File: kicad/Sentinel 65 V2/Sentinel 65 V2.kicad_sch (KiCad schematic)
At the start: 159 parts, among them J1 SNES Controller, J10 SVGA Connector, J11 USB_C_Receptacle_PowerOnly_6P, J12 Conn_01x02, J13 Conn_01x02, J14 Internal Control Header (Opti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, J15 Conn_02x11_Odd_Even, J2 2x32 2.54mm Card Edge Connect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, J3 Conn_02x12_Odd_Even, J4 SNES Controller, J5 SD_Card, J6 LEFT, J7 FPGA_PROG, J8 RIGHT, J9 Flash Enable, SW1 SW_Push, SW2 SW_Push, SW3 SW_Push, U1 ATF22LV10C, U10 LM1086IT-3.3, U11 MCP1316MT-33LE/OT, U2 W65C265S8PLG-8, U3 IS61WV5128EDBLL-10TLI, U4 SST39LF040-55-4C-NHE-T, U5 W25Q16JVSNIQ, U6 AP7361C-12E, U7 74CBTLV3126PW,118, U8 ICE40UP5K-SG48ITR, U9 WM8524CGEDT, X1 32.768KHz, X2 8Mhz, X3 25MHz

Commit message: Added audio mixing of cartridge audio
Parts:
- removed C26: 1µF, Capacitor_SMD:C_0402_1005Metric, symbol Device:C
- removed C27: 2.7nf, Capacitor_SMD:C_0402_1005Metric, symbol Device:C
- removed C29: 2.2µF, Capacitor_SMD:C_0402_1005Metric, symbol Device:C
- removed C31, C32: 4.7µF, Capacitor_SMD:C_0402_1005Metric, symbol Device:C
- removed D1, D2: PESD3V3L1BA-N, Diode_SMD:D_SOD-323, symbol Diode:PESD3V3L1BA-N
- removed J6: LEFT, symbol Connector:Conn_Coaxial
- removed J8: RIGHT, symbol Connector:Conn_Coaxial
- removed J9: Flash Enable, Connector_PinHeader_2.54mm:PinHeader_1x02_P2.54mm_Vertical, symbol Connector_Generic:Conn_01x02
- removed JP1: Jumper_3_Open, Jumper:SolderJumper-3_P2.0mm_Open_TrianglePad1.0x1.5mm_NumberLabels, symbol Jumper:Jumper_3_Open
- removed R12, R19: 560Ω, Resistor_SMD:R_0402_1005Metric, symbol Device:R
- removed R24, R48: 3.3kΩ, Resistor_SMD:R_0402_1005Metric, symbol Device:R
- added C26, C27, C29, C31, C32, C33: 2.2µF, symbol Device:C_Polarized
- added C34: 2.2µF, Capacitor_SMD:C_0402_1005Metric, symbol Device:C
- added C35: 1µF, Capacitor_SMD:C_0402_1005Metric, symbol Device:C
- added C36, C37: 4.7µF, Capacitor_SMD:C_0402_1005Metric, symbol Device:C
- added D10, D11: PESD3V3L1BA-N, Diode_SMD:D_SOD-323, symbol Diode:PESD3V3L1BA-N
- added J12: LEFT, symbol Connector:Conn_Coaxial
- added J13: RIGHT, symbol Connector:Conn_Coaxial
- added JP1: SolderJumper_3_Bridged12, Jumper:SolderJumper-3_P1.3mm_Bridged12_RoundedPad1.0x1.5mm, symbol Jumper:SolderJumper_3_Bridged12
- added R57, R58, R60, R61: 3.3kΩ, Resistor_SMD:R_0402_1005Metric, symbol Device:R
- added R71, R72, R73, R74, R75, R76: 1kΩ, Resistor_SMD:R_0402_1005Metric, symbol Device:R
- added U10: TLV9062xD, Package_SO:SOIC-8_3.9x4.9mm_P1.27mm, symbol Amplifier_Operational:TLV9062xD
- C28: value 2.7nF -> 1µF
- C30: value 1µF -> 100nF
- J10: renamed from J13; now fitted; now in the parts list
- J11: renamed from J12; now fitted; now in the parts list
- renumbered C37 to C38, C33 to C39, C34 to C40, C35 to C41, C36 to C42, C8 to C5, C5 to C8, D6 to D1, D8 to D2, D7 to D3, D9 to D4, D13 to D5, D12 to D6, D3 to D7, D4 to D8, D5 to D9, H6 to H1, H5 to H2, H4 to H3, H3 to H4, H2 to H5, H1 to H6, J11 to J14, J4 to J2, J2 to J3, J3 to J4, J14 to J5, J15 to J6, J5 to J7, J7 to J8, J10 to J9, R13 to R12, R14 to R13, R15 to R14, R16 to R15, R17 to R16, R18 to R17, R26 to R18, R25 to R19, R28 to R24, R27 to R25, R31 to R26, R29 to R27, R30 to R28, R37 to R29, R32 to R30, R64 to R31, R65 to R32, R66 to R33, R67 to R34, R60 to R35, R62 to R36, R33 to R37, R34 to R38, R35 to R39, R36 to R40, R43 to R41, R38 to R42, R39 to R43, R40 to R44, R41 to R45, R42 to R46, R45 to R47, R44 to R48, R61 to R49, R63 to R50, R68 to R51, R69 to R52, R70 to R53, R71 to R54, R47 to R55, R46 to R56, R49 to R59, R50 to R62, R51 to R63, R52 to R64, R53 to R65, R72 to R66, R54 to R67, R55 to R68, R56 to R69, R57 to R70, R58 to R77, R59 to R78, SW3 to SW1, SW1 to SW3, U10 to U11, U11 to U12, U4 to U2, U2 to U3, U3 to U4
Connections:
- net ~{FLASH_EN} is gone; now on net ~{IRQ}3: U1.13 (IN)
- net +3.3V: now also C30.1, C36.1, C37.1, R57.1, R58.1, U10.8 (V+)
- net A19: now also U1.8 (IN); no longer U1.9 (IN)
- net A20: now also U1.9 (IN); no longer U1.10 (IN)
- net A21: now also U1.10 (IN); no longer U1.11 (IN)
- net A5: now also U1.7 (IN)
- net BE: now also J3.a21 (Pin_a21)
- net D0: now also J3.b15 (Pin_b15); no longer J3.b20 (Pin_b20)
- net D1: now also J3.a15 (Pin_a15); no longer J3.a20 (Pin_a20)
- net D2: now also J3.b16 (Pin_b16); no longer J3.b21 (Pin_b21)
- net D3: now also J3.a16 (Pin_a16); no longer J3.a21 (Pin_a21)
- net D4: now also J3.b17 (Pin_b17); no longer J3.b22 (Pin_b22)
- net D5: now also J3.a17 (Pin_a17); no longer J3.a22 (Pin_a22)
- net D6: now also J3.b18 (Pin_b18); no longer J3.b23 (Pin_b23)
- net D7: now also J3.a19 (Pin_a19); no longer J3.a23 (Pin_a23)
- net GND: now also C34.2, C35.2, C36.2, C37.2, D10.1 (A1), D11.1 (A1), J12.2 (Ext), J13.2 (Ext), R60.1, R61.1, U10.3 (+), U10.4 (V-), U10.5 (+); no longer C28.2
- net I2C_SCL: now also R57.2
- net I2C_SDA: now also R58.2
- net IRQ3: now also U1.22 (I/O), R61.2; no longer U1.23 (I/O)
- net PHI2: now also JP1.2 (C)
- net PXCLK: now also JP1.3 (B)
- net VCLK: now also JP1.1 (A)
- net ~{CLOCK}: now also U1.20 (I/O); no longer U3.51 (~{CS1})
- net ~{EXP}: now also J3.a20 (Pin_a20); no longer J3.b17 (Pin_b17)
- net ~{IRQ}2: now also U3.3 (~{NE57}); no longer U1.7 (IN)
- net ~{IRQ}3: no longer U1.8 (IN)
- net ~{RAM}: now also J3.a22 (Pin_a22); no longer J3.b19 (Pin_b19)
- net ~{RD}: now also J3.b20 (Pin_b20); no longer J3.a16 (Pin_a16)
- net ~{ROM}0: now also J3.b21 (Pin_b21)
- net ~{ROM}1: now also J3.b22 (Pin_b22), R47.2; no longer J3.b18 (Pin_b18)
- net ~{VERA}: now also J3.b23 (Pin_b23), U1.21 (I/O); no longer U3.50 (~{CS0})
- net ~{WR}: now also J3.b19 (Pin_b19); no longer J3.b16 (Pin_b16)
- net at U9.3 (CPCB): now also C28.1
- net at U9.5 (CPCA): now also C28.2
- net RUN: now reaches U3.14 (RUN)
- net RUN: now also J3.a23 (Pin_a23)
- net VIRQ: now reaches J3.a26 (Pin_a26)
- net VIRQ: now also U3.2 (PE56), U8.32 (IOT_43a), R60.2
- net CART_L: now reaches J3.b31 (Pin_b31)
- net CART_L: now also C27.1
- net CART_R: now reaches J3.b32 (Pin_b32)
- net CART_R: now also C32.1
- net DAC_R: now reaches U9.16 (LINEVOUTR)
- net DAC_R: now also C33.1
- net DAC_L: now reaches U9.1 (LINEVOUTL)
- net DAC_L: now also C29.1
- net at U9.14 (VMID): now also C34.1
- net at U9.2 (CPVOUTN): now also C35.1; no longer C30.1
- removed net IRQ2: U1.22 (I/O), U3.2 (PE56)
- net ~{IRQ} renamed ~{IRQ}0
- removed net ~{VIRQ}: R47.2, U3.3 (~{NE57}), U8.32 (IOT_43a)
- new net: C27.2, R71.2
- new net: C32.2, R74.2
- new net: R74.1, R75.1, R76.2, U10.6 (-)
- new net: C31.1, R76.1, U10.7
- new net: R71.1, R72.1, R73.2, U10.2 (-)
- new net: C31.2, D11.2 (A2), J13.1 (In)
- new net: C26.1, R73.1, U10.1
- new net: C29.2, R72.2
- new net: C26.2, D10.2 (A2), J12.1 (In)
- new net: C33.2, R75.2
- new net ~{IO}1: U1.11 (IN), U3.51 (~{CS1})
- no-connect marks 22 -> 14
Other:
- note added: "Audio Mixer & Output"
- note added: "Future DV board options may need to use the pixel clock from the VERA directly; to prepare for that eventuality, a solderable jumper is provided which can be used to disconnect PHI2 from the VERA, and connect that pin to the DV header."
- note added: "I2S DAC"
- note added: "The Amiga inspired clock port serves double duty as the debug port."
- note added: "The cartridge port is mechanically and electrically, but not logically, compatible with cartridges from the Sega Mega Drive/Genesis console."
- note added: "The system ROM is a PLCC32 in an SMD socket."
- note added: "This button will eventually be sensed by the boot ROM, and will enable a maintenance mode which allows reflashing the ROMs."
- note added: "This revision of the design uses a PLCC-84 CPU and a DIP GAL, because they are what I have in stock at the moment. The next revision will switch those to equivalent parts in SMD packages: QFP-100 for the CPU, PLCC for the ATF22LV10C."
- note added: "Twin RCA connectors output line-level stereo audio, Amiga-style, mixed from the I2C DAC and whatever the cartridge outputs on its output lines."
- note removed: "I2S DAC & Stereo Output"
- note removed: "This revision of the design uses a PLCC-84 CPU and a DIP GAL, because they are what I have in stock at the moment. The next revision will switch those to equivalent parts in QFP-type packages."
- note removed: "Twin RCA connectors output line-level stereo audio, Amiga-style."
- note removed: "~{RD} = PHI2 NAND R/~{W} ~{WR} = (NOT PHI1) NAND R/~{W} ~{SD_SS} = CDONE AND NOT ~{FPGA_SS} ~{FLASH_SS} = NOT CDONE and NOT ~{FPGA_SS} ~{IRQ}2 = NOT IRQ2 ~{IRQ}3 = NOT IRQ3 ~{ROM}0 = ~{LOROM} XOR ~{HIROM} ~{ROM}1 = ADDRESS >= $C80000"
- moved on the sheet: C38, C39, C40, C41, C42, C5, C8, C9, H1, H2, H3, H4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

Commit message: logo import
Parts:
- removed J10: Conn_01x02, symbol Connector_Generic:Conn_01x02
- removed R58: 3.3kΩ, Resistor_SMD:R_0402_1005Metric, symbol Device:R
- removed SW2: SW_Push, symbol Switch:SW_Push
- added D1: LED5, symbol Device:LED
- added J15: Conn_01x02, symbol Connector_Generic:Conn_01x02
- added R37: 1kΩ, Resistor_SMD:R_0402_1005Metric, symbol Device:R
- added R70: 3.3kΩ, Resistor_SMD:R_0402_1005Metric, symbol Device:R
- C27: renamed from C26; value 2.2µF -> 2.2µF 0.1%
- C28: renamed from C27; value 2.2µF -> 2.2µF 0.1%
- C30: renamed from C29; value 2.2µF -> 2.2µF 0.1%
- C32: renamed from C31; value 2.2µF -> 2.2µF 0.1%
- C33: renamed from C32; value 2.2µF -> 2.2µF 0.1%
- C34: renamed from C33; value 2.2µF -> 2.2µF 0.1%
- R72: renamed from R71; value 1kΩ -> 1kΩ 0.1%
- R73: renamed from R72; value 1kΩ -> 1kΩ 0.1%
- R74: renamed from R73; value 1kΩ -> 1kΩ 0.1%
- R75: renamed from R74; value 1kΩ -> 1kΩ 0.1%
- R76: renamed from R75; value 1kΩ -> 1kΩ 0.1%
- R77: renamed from R76; value 1kΩ -> 1kΩ 0.1%
- renumbered C9 to C10, C24 to C11, C11 to C12, C12 to C13, C13 to C14, C14 to C15, C15 to C16, C16 to C17, C17 to C18, C18 to C19, C19 to C20, C20 to C21, C21 to C22, C22 to C23, C23 to C24, C28 to C29, C30 to C31, C34 to C35, C35 to C36, C36 to C37, C37 to C38, C38 to C39, C39 to C40, C40 to C41, C41 to C42, C42 to C43, C10 to C9, D9 to D10, D10 to D12, D11 to D13, D5 to D2, D6 to D3, D1 to D4, D2 to D5, D7 to D6, D8 to D7, D3 to D8, D4 to D9, J11 to J10, J4 to J3, J3 to J4, R3 to R1, R12 to R10, R13 to R11, R14 to R12, R15 to R13, R20 to R14, R21 to R15, R22 to R16, R23 to R17, R9 to R18, R10 to R19, R4 to R2, R28 to R20, R16 to R21, R17 to R22, R37 to R23, R38 to R24, R39 to R25, R40 to R26, R18 to R27, R19 to R28, R43 to R29, R5 to R3, R44 to R30, R45 to R31, R46 to R32, R24 to R33, R25 to R34, R26 to R35, R27 to R36, R29 to R38, R30 to R39, R6 to R4, R31 to R40, R32 to R41, R33 to R42, R34 to R43, R59 to R44, R41 to R45, R42 to R46, R62 to R47, R63 to R48, R64 to R49, R7 to R5, R65 to R50, R35 to R51, R36 to R52, R47 to R53, R48 to R54, R67 to R55, R68 to R56, R69 to R57, R70 to R58, R51 to R59, R1 to R6, R52 to R60, R53 to R61, R54 to R62, R49 to R63, R50 to R64, R55 to R65, R56 to R66, R57 to R67, R60 to R68, R61 to R69, R2 to R7, R66 to R71, R77 to R78, R78 to R79, R11 to R9, U7 to U6, U6 to U7
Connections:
- net +3.3V: now also R70.1
- net BE: now also R39.2; no longer R46.2
- net GND: now also D1.1 (K)
- net I2C_SDA: now also R66.2
- net ~{BOOT_SEL}: now also J15.1 (Pin_1), R37.2
- net ~{IRQ}4: now also R36.2; no longer R39.2
- net ~{NMI}: now also R70.2; no longer R36.2
- net ~{RAM}: now also R46.2; no longer R54.2
- net ~{ROM}0: now also R54.2; no longer R66.2
- net at R71.1, SW1.2: now also J15.2 (Pin_2)
- new net: D1.2 (A), R37.1
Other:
- note added: "Mounting Holes"
- note removed: "NMI Button"
- moved on the sheet: C10, C11, C25, C31, C9, D10, D2, D3, D4, D5, D6, D7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

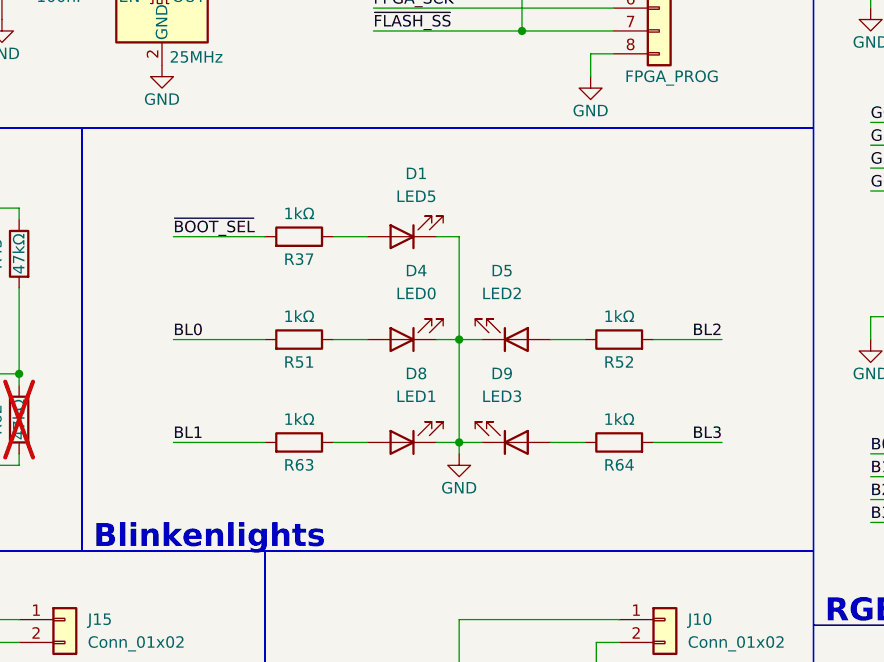
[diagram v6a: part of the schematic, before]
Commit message: Updated schematic PDF
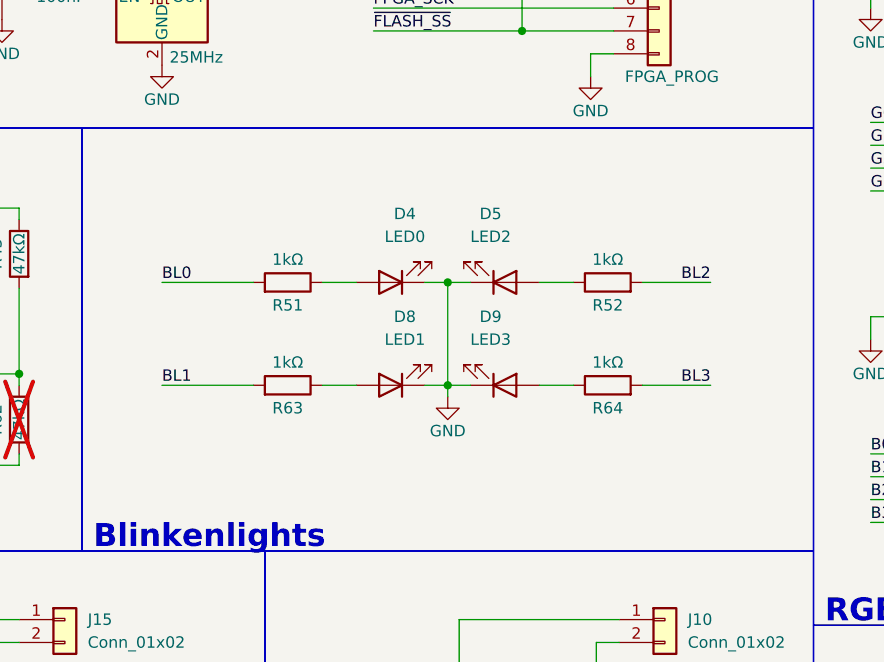
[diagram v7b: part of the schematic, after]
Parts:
- removed D1: LED5, symbol Device:LED
- removed R37: 1kΩ, Resistor_SMD:R_0402_1005Metric, symbol Device:R
- U3: footprint Package_LCC:PLCC-84_THT-Socket -> Package_LCC:PLCC-84_SMD-Socket
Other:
- moved on the sheet: D4, D5, D8, D9, R51, R52, R63, R64

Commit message: Updated license terms
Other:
- note added: "This source describes Open Hardware and is licensed under the CERN-OHL-P v2. You may redistribute and modify this documentation and make products using it under the terms of the CERN-OHL-P v2 (https:/cern.ch/cern-ohl). This documentation is distributed WITHOUT ANY EXPRESS OR IMPLIED WARRANTY, INCLUDING OF MERCHANTABILITY, SATISFACTORY QUALITY AND FITNESS FOR A PARTICULAR PURPOSE. Please see the C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"
- title: Sentinel 65X -> Sentinel 65X V2 Rev0
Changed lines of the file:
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@@
   (paper "User" 550.012 424.993)
   (title_block
-    (title "Sentinel 65X")
-    (date "2023-12-10")
+    (title "Sentinel 65X V2 Rev0")
+    (date "2023-12-16")
     (rev "0")
     (company "Studio 8502")
-    (comment 1 "Released under the terms of the MIT license")
+    (comment 1 "Licensed under CERN-OHL-P v2")
     (comment 2 "Copyright © 2023 Kyle J Cardoza, Studio 8502")
     (comment 3 "Dedicated to the memory of Earl William \"Madman\" Muntz")
@@
     (effects (font (size 2.54 2.54) (thickness 0.508) bold) (justify left bottom))
   )
+  (text "This source describes Open Hardware and is licensed under the \nCERN-OHL-P v2. You may redistribute and modify this documentation \nand make products using it under the terms of the CERN-OHL-P v2 \n(https:/cern.ch/cern-ohl). This documentation is distributed \nWITHOUT ANY EXPRESS OR IMPLIED WARRANTY, INCLUDING OF \nMERCHANTABILITY, SATISFACTORY QUALITY AND FITNESS FOR A \nPARTICULAR PURPOSE. Please see the CERN-OHL-P v2 for applicable \nconditions"
+    (at 356.87 410.845 0)
+    (effects (font (size 1.27 1.27)) (justify left bottom))
+  )
   (text "This button will eventually be sensed by\nthe boot ROM, and will enable a maintenance\nmode which allows reflashing the ROMs."
